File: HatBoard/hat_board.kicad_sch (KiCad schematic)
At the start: 0 parts

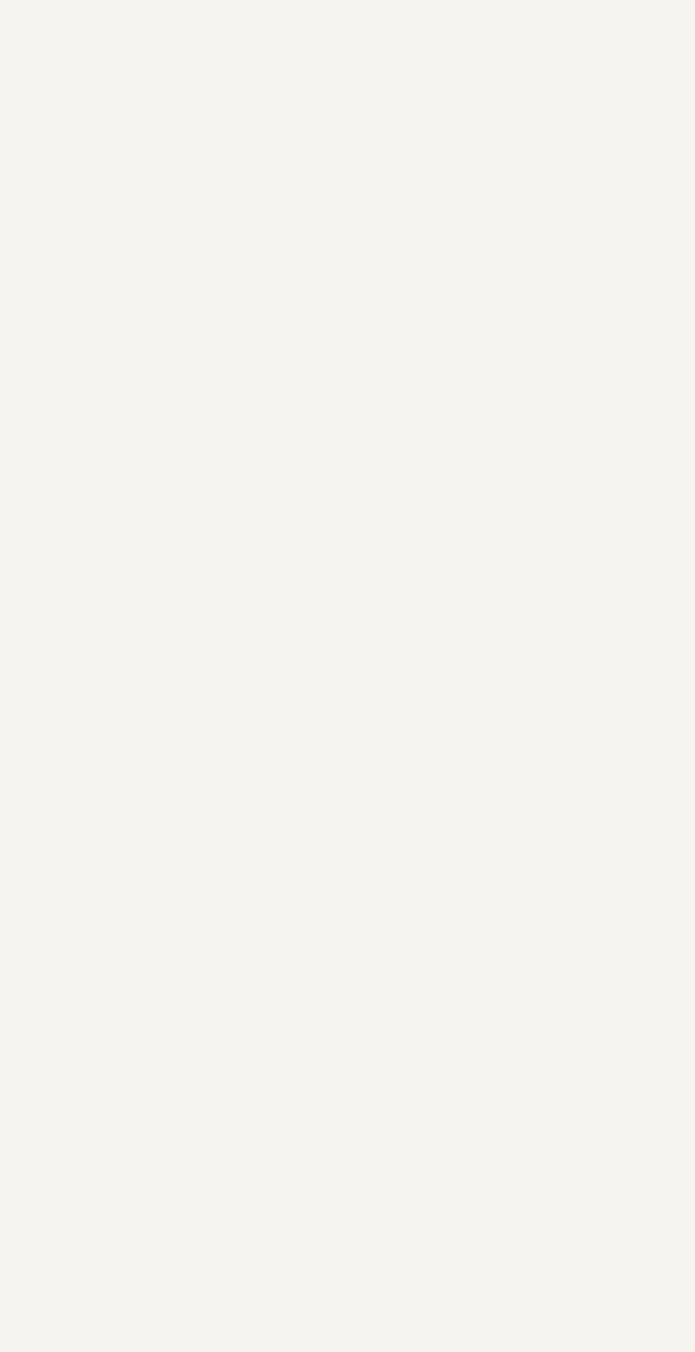
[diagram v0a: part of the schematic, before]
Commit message: changed so only one set of sensors (save money)
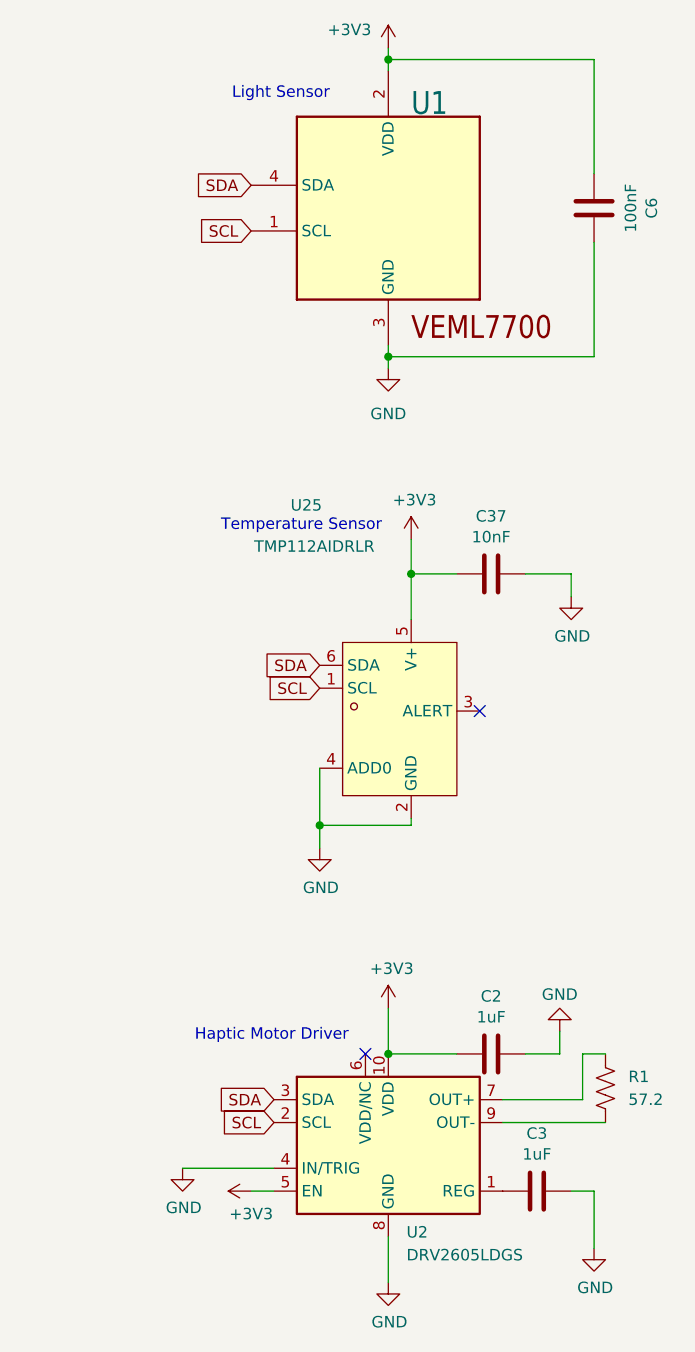
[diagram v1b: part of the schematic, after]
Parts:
- added C2, C3: 1uF, Capacitor_SMD:C_0805_2012Metric, symbol Device:C
- added C37: 10nF, Capacitor_SMD:C_0402_1005Metric, symbol Device:C
- added C6: 100nF, Capacitor_SMD:C_0402_1005Metric, symbol Device:C
- added R1: 57.2, Resistor_SMD:R_0201_0603Metric_Pad0.64x0.40mm_HandSolder, symbol Device:R_US
- added U1: VEML7700, easyeda2kicad:SENSOR-SMD_EML7700-TT, symbol Adafruit VEML7700-eagle-import:VEML7700
- added U2: DRV2605LDGS, Package_SO:VSSOP-10_3x3mm_P0.5mm, symbol Driver_Haptic:DRV2605LDGS
- added U25: TMP112AIDRLR, easyeda2kicad:SOT-563_L1.6-W1.2-P0.50-LS1.6-BR, symbol easyeda2kicad:TMP112AIDRLR
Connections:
- new net: C3.1, U2.1 (REG)
- new net: R1.1, U2.7 (OUT+)
- new net: R1.2, U2.9 (OUT-)
- new net +3V3: C2.1, C37.1, C6.1, U1.2 (VDD), U2.10 (VDD), U2.5 (EN), U25.5 (V+)
- new net GND: C2.2, C3.2, C37.2, C6.2, U1.3 (GND), U2.4 (IN/TRIG), U2.8 (GND), U25.2 (GND), U25.4 (ADD0)
- new net SCL: U1.1 (SCL), U2.2 (SCL), U25.1 (SCL)
- new net SDA: U1.4 (SDA), U2.3 (SDA), U25.6 (SDA)
- no-connect marks 0 -> 2
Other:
- note added: "Haptic Motor Driver"
- note added: "Light Sensor"
- note added: "Temperature Sensor"

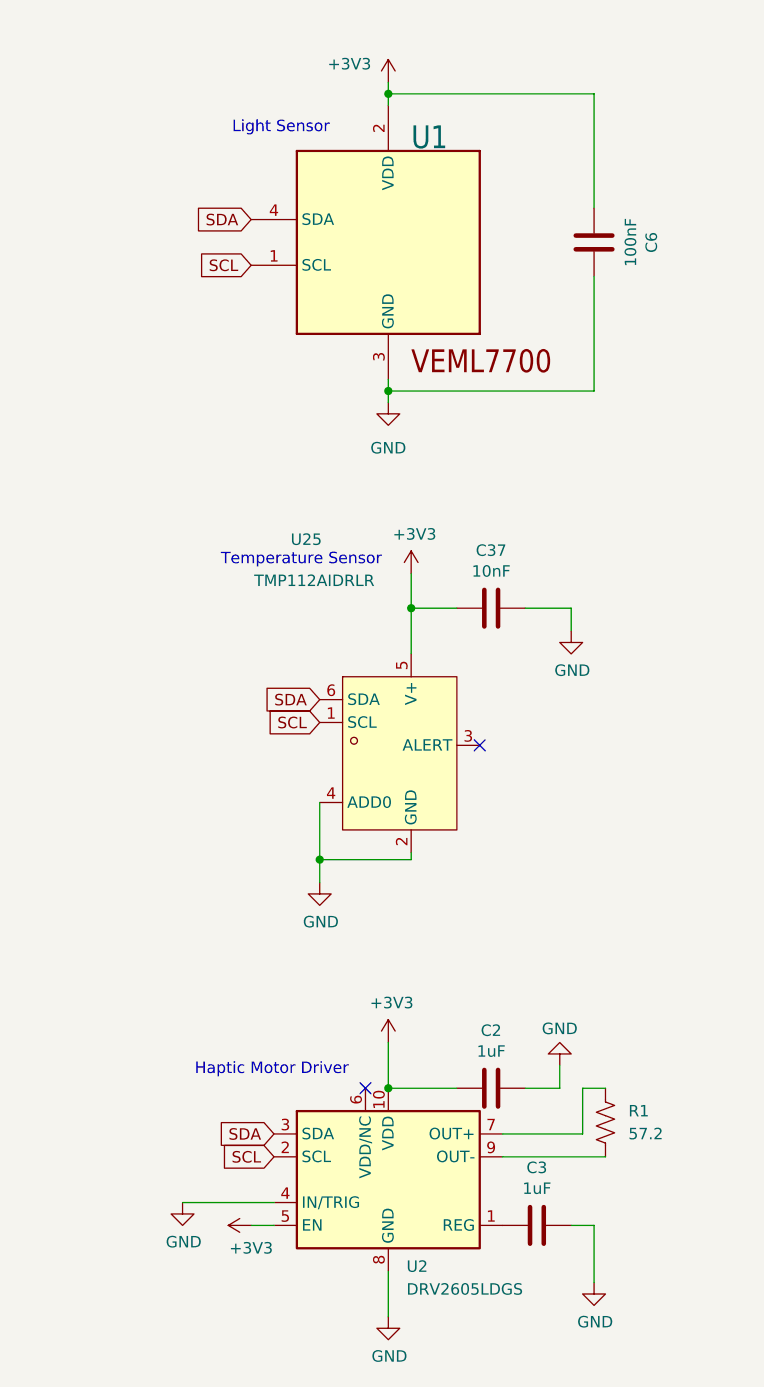
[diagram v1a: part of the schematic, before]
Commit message: changed so only one set of sensors and each has own bus
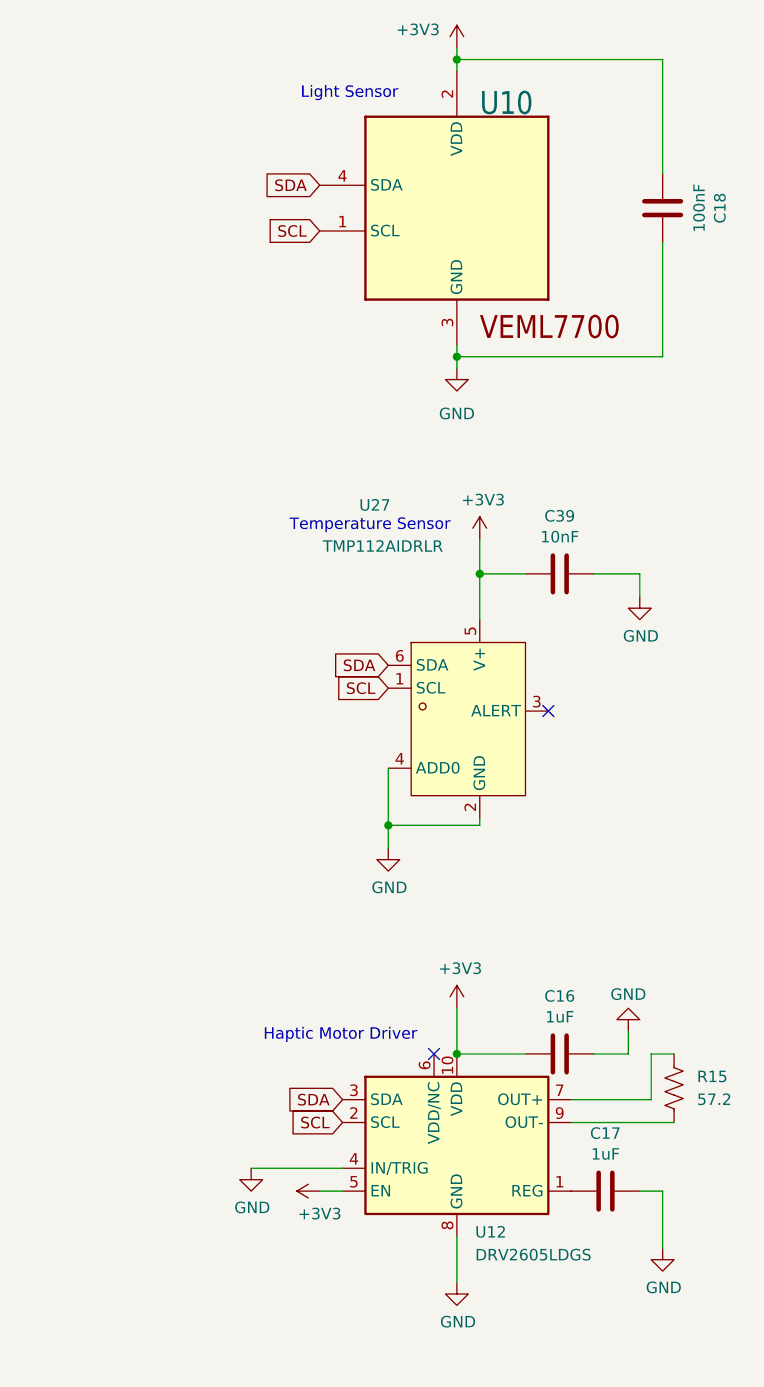
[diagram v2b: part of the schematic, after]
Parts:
- renumbered C2 to C16, C3 to C17, C6 to C18, C37 to C39, R1 to R15, U1 to U10, U2 to U12, U25 to U27
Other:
- moved on the sheet: C16, C17, C18, C39, R15, U10, U12, U27

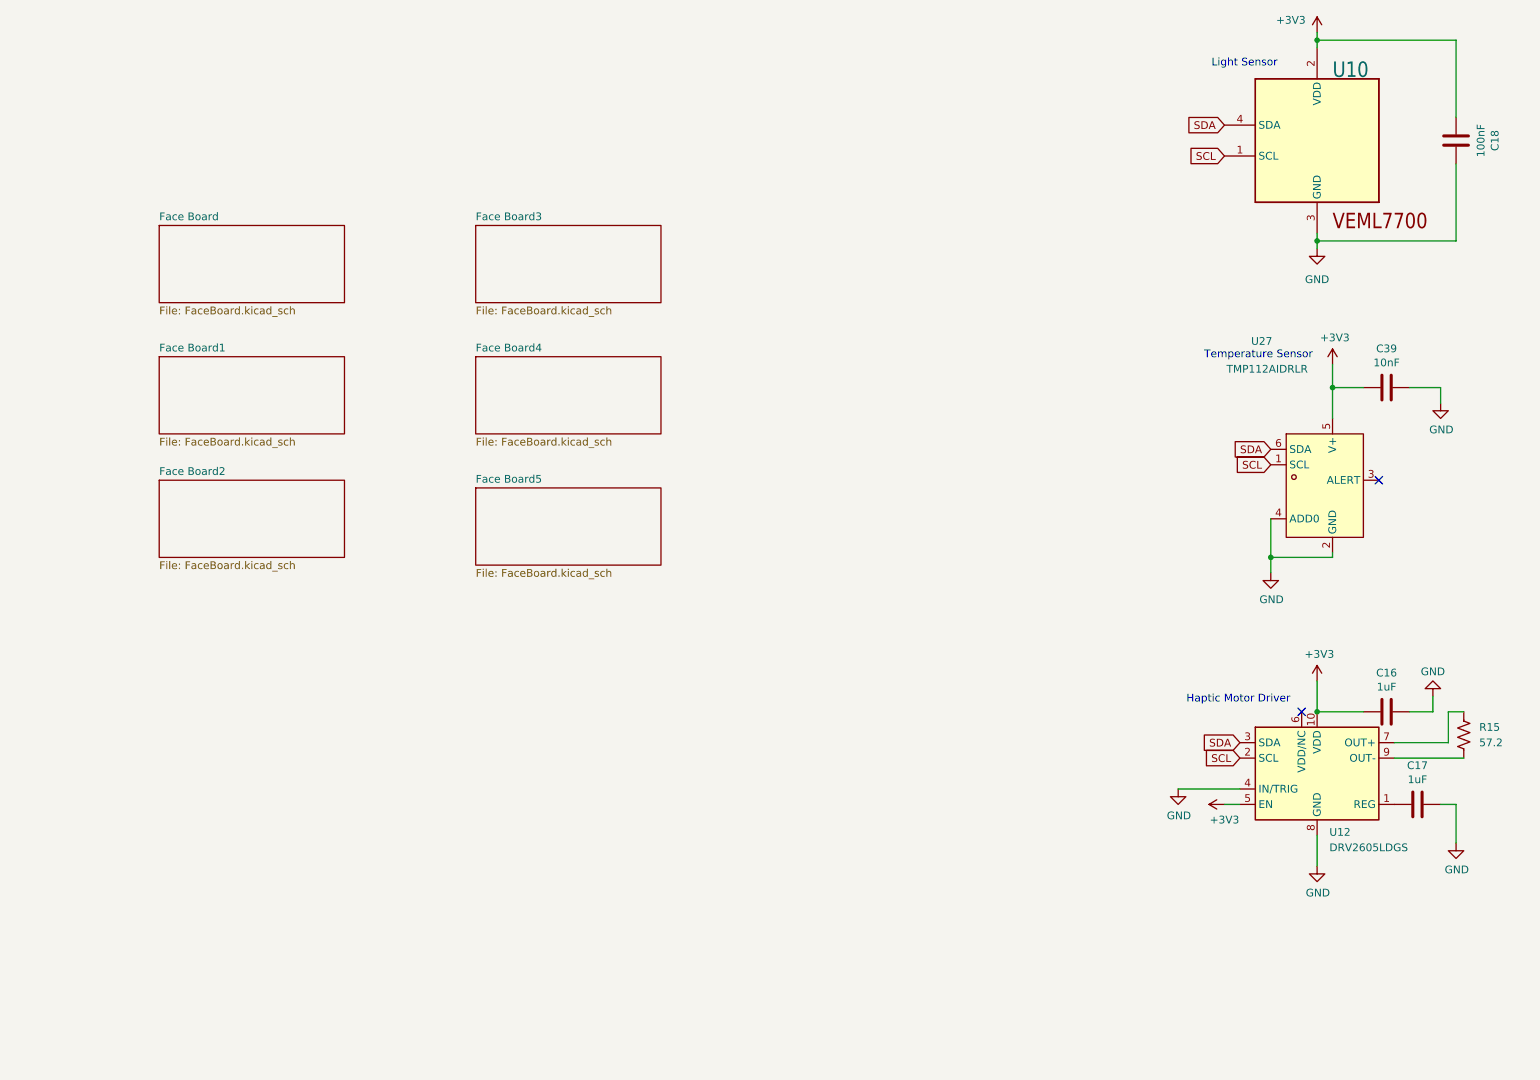
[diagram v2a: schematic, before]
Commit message: fixed the electrical rules checking
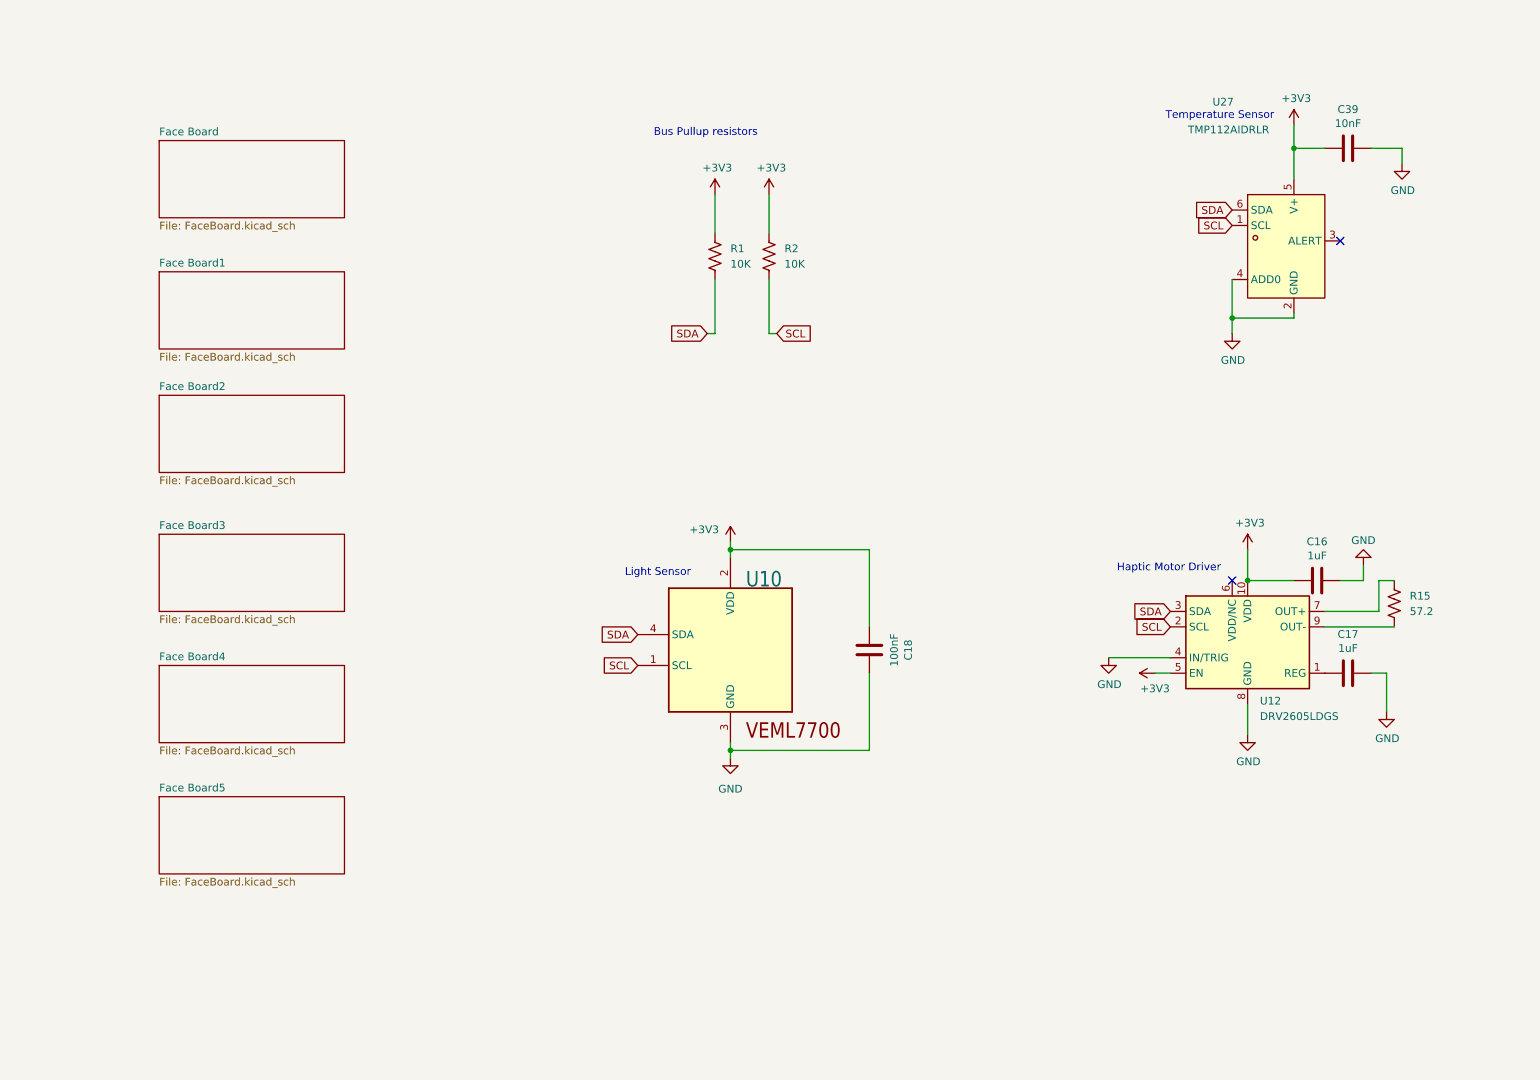
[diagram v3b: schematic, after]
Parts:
- added R1, R2: 10K, symbol Device:R_US
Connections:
- net +3V3: now also R1.2, R2.2
- net SCL: now also R2.1
- net SDA: now also R1.1
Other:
- note added: "Bus Pullup resistors"
- moved on the sheet: C16, C17, C18, C39, R15, U10, U12, U27

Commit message: added modifications for 2 cables
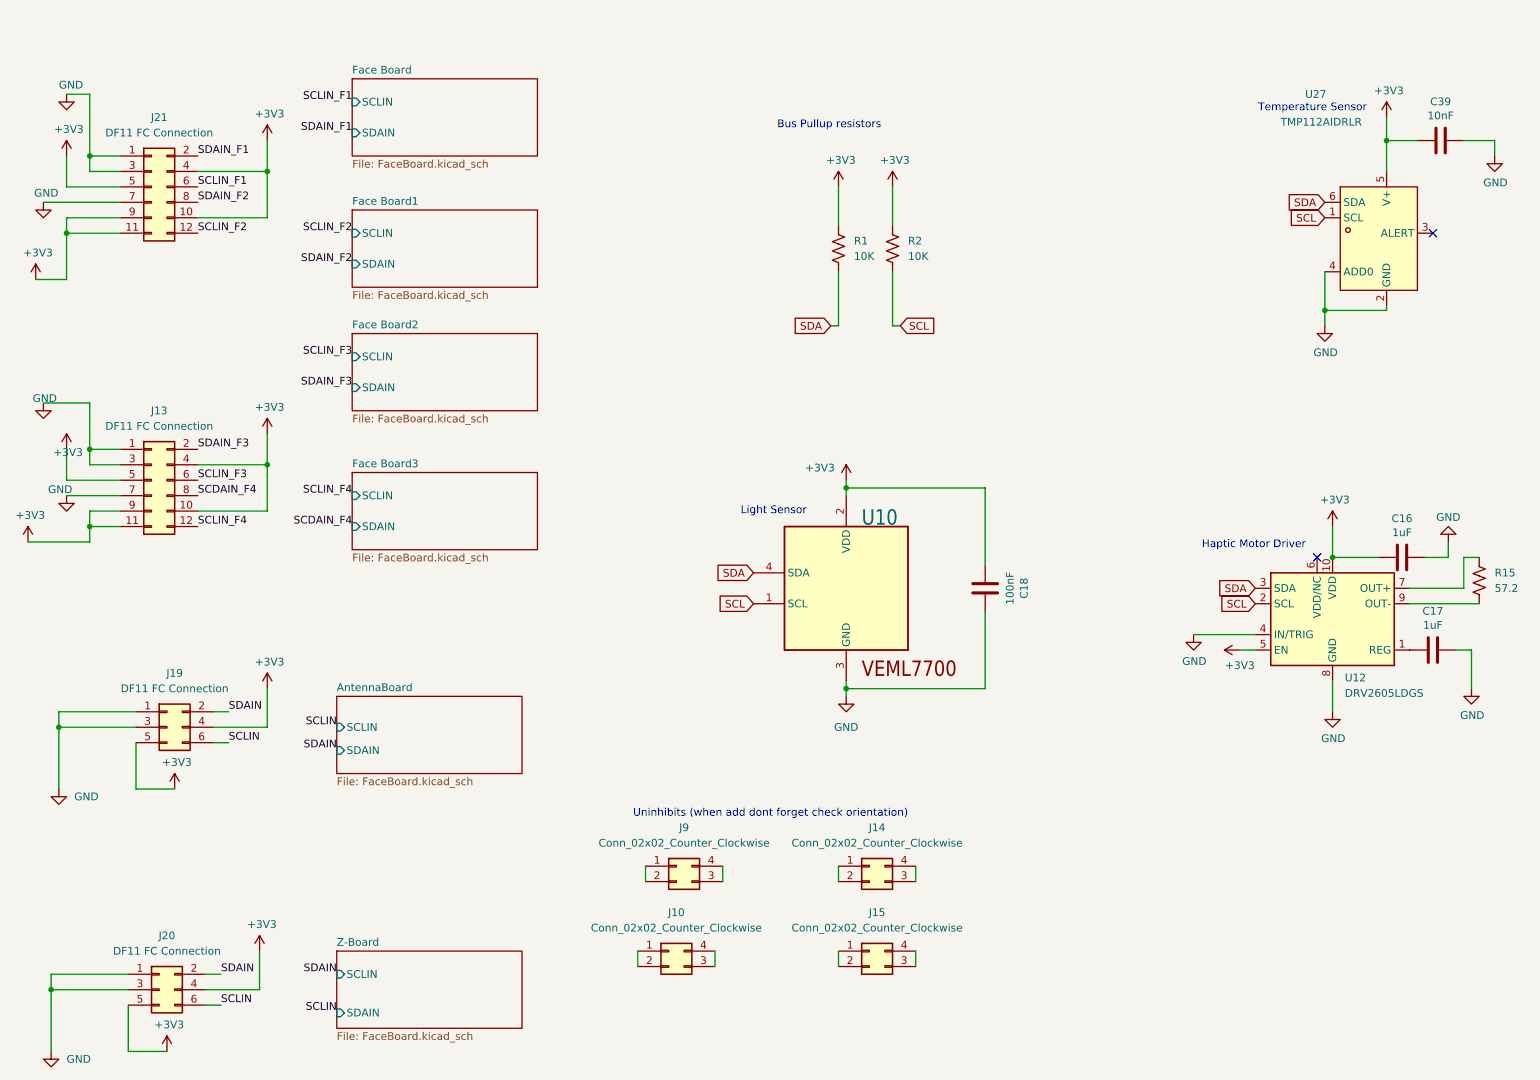
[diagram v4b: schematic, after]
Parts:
- added J10, J14, J15, J9: Conn_02x02_Counter_Clockwise, symbol Connector_Generic:Conn_02x02_Counter_Clockwise
- added J13, J21: DF11 FC Connection, symbol Connector_Generic:Conn_02x06_Odd_Even
- added J19, J20: DF11 FC Connection, symbol Connector_Generic:Conn_02x03_Odd_Even
- R1, R2: footprint (none) -> Resistor_SMD:R_0603_1608Metric
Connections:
- net +3V3: now also J13.10 (Pin_10), J13.11 (Pin_11), J13.4 (Pin_4), J13.5 (Pin_5), J13.9 (Pin_9), J19.4 (Pin_4), J19.5 (Pin_5), J20.4 (Pin_4), J20.5 (Pin_5), J21.10 (Pin_10), J21.11 (Pin_11), J21.4 (Pin_4), J21.5 (Pin_5), J21.9 (Pin_9)
- net GND: now also J13.1 (Pin_1), J13.3 (Pin_3), J13.7 (Pin_7), J19.1 (Pin_1), J19.3 (Pin_3), J20.1 (Pin_1), J20.3 (Pin_3), J21.1 (Pin_1), J21.3 (Pin_3), J21.7 (Pin_7)
- new net: J9.1 (Pin_1), J9.2 (Pin_2)
- new net: J9.3 (Pin_3), J9.4 (Pin_4)
- new net: J15.1 (Pin_1), J15.2 (Pin_2)
- new net: J15.3 (Pin_3), J15.4 (Pin_4)
- new net: J14.1 (Pin_1), J14.2 (Pin_2)
- new net: J14.3 (Pin_3), J14.4 (Pin_4)
- new net: J10.1 (Pin_1), J10.2 (Pin_2)
- new net: J10.3 (Pin_3), J10.4 (Pin_4)
- new net SCDAIN_F4: J13.8 (Pin_8)
- new net SCLIN: J19.6 (Pin_6), J20.6 (Pin_6)
- new net SCLIN_F1: J21.6 (Pin_6)
- new net SCLIN_F2: J21.12 (Pin_12)
- new net SCLIN_F3: J13.6 (Pin_6)
- new net SCLIN_F4: J13.12 (Pin_12)
- new net SDAIN: J19.2 (Pin_2), J20.2 (Pin_2)
- new net SDAIN_F1: J21.2 (Pin_2)
- new net SDAIN_F2: J21.8 (Pin_8)
- new net SDAIN_F3: J13.2 (Pin_2)
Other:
- sheet Face Board4 renamed AntennaBoard
- sheet Face Board5 renamed Z-Board
- sheet AntennaBoard ports: added SCLIN, SDAIN; removed none
- sheet Face Board ports: added SCLIN, SDAIN; removed none
- sheet Face Board1 ports: added SCLIN, SDAIN; removed none
- sheet Face Board2 ports: added SCLIN, SDAIN; removed none
- sheet Face Board3 ports: added SCLIN, SDAIN; removed none
- sheet Z-Board ports: added SCLIN, SDAIN; removed none
- note added: "Uninhibits (when add dont forget check orientation)"
- moved on the sheet: C16, C17, C18, C39, R1, R15, R2, U10, U12, U27
